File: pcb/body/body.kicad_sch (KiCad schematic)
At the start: 3 parts, among them J1 Conn_01x08_Socket, J2 Conn_01x05_Pin, U1 Teensy4.1

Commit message: output stage
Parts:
- removed U1: Teensy4.1, symbol teensy:Teensy4.1
- added A1: Electrosmith_Daisy_Seed_Rev4, Module:Electrosmith_Daisy_Seed, symbol MCU_Module:Electrosmith_Daisy_Seed_Rev4
- added J3, J4: AudioJack2, symbol Connector_Audio:AudioJack2
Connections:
- net GND: now also J3.S, J4.S
- net PICKUP_1: now also A1.22 (ADC_0)
- new net PICKUP_2: A1.23 (ADC_1)
- new net PICKUP_3: A1.24 (ADC_2)
- new net PICKUP_4: A1.25 (ADC_3)
- new net PICKUP_5: A1.26 (ADC_4)
- new net PICKUP_6: A1.27 (ADC_5)
- new net outputstage/INPUT_1: A1.18 (AUDIO_OUT_1)
- new net outputstage/INPUT_2: A1.19 (AUDIO_OUT_2)
- new net outputstage/OUTPUT_1: J3.T
- new net outputstage/OUTPUT_2: J4.T
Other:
- added sheet outputstage (outputstage.kicad_sch)
- moved on the sheet: J1

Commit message: pcb stuff
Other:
- added sheet codec1 (codec.kicad_sch)
- added sheet codec2 (codec.kicad_sch)
- added sheet codec3 (codec.kicad_sch)
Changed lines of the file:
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@@
+    )
+  )
+  (sheet (at 27.94 111.76) (size 27.94 15.24) (fields_autoplaced)
+    (stroke (width 0.1524) (type solid))
+    (fill (color 0 0 0 0.0000))
+    (property "Sheetname" "codec1" (at 27.94 111.0484 0)
+      (effects (font (size 1.27 1.27)) (justify left bottom))
+    )
+    (property "Sheetfile" "codec.kicad_sch" (at 27.94 127.5846 0)
+      (effects (font (size 1.27 1.27)) (justify left top))
+    )
+    (pin "LINE_IN_L" input (at 27.94 114.3 180)
+      (effects (font (size 1.27 1.27)) (justify left))
+    )
+    (pin "DAC_DOUT" output (at 55.88 114.3 0)
+      (effects (font (size 1.27 1.27)) (justify right))
+    )
+    (pin "DAC_DIN" input (at 55.88 116.84 0)
+      (effects (font (size 1.27 1.27)) (justify right))
+    )
+    (pin "LINE_IN_R" input (at 27.94 116.84 180)
+      (effects (font (size 1.27 1.27)) (justify left))
+    )
+    (pin "LINE_OUT_R" output (at 27.94 119.38 180)
+      (effects (font (size 1.27 1.27)) (justify left))
+    )
+    (pin "LINE_OUT_L" output (at 27.94 121.92 180)
+      (effects (font (size 1.27 1.27)) (justify left))
+    )
+    (instances
+      (project "body"
+        (path "/392bd065-a607-4eff-83a3-798a3e7c56fd" (page "6"))
+      )
     )
   )
@@
       )
     )
+  )
+  (sheet (at 27.94 133.35) (size 27.94 15.24) (fields_autoplaced)
+    (stroke (width 0.1524) (type solid))
+    (fill (color 0 0 0 0.0000))
+    (property "Sheetname" "codec2" (at 27.94 132.6384 0)
+      (effects (font (size 1.27 1.27)) (justify left bottom))
+    )
+    (property "Sheetfile" "codec.kicad_sch" (at 27.94 149.1746 0)
+      (effects (font (size 1.27 1.27)) (justify left top))
+    )
+    (instances
+      (project "body"
+        (path "/392bd065-a607-4eff-83a3-798a3e7c56fd" (page "7"))
+      )
+    )
+  )
+  (sheet (at 27.94 154.94) (size 27.94 15.24) (fields_autoplaced)
+    (stroke (width 0.1524) (type solid))
+    (fill (color 0 0 0 0.0000))
+    (property "Sheetname" "codec3" (at 27.94 154.2284 0)
+      (effects (font (size 1.27 1.27)) (justify left bottom))
+    )
+    (property "Sheetfile" "codec.kicad_sch" (at 27.94 170.7646 0)
+      (effects (font (size 1.27 1.27)) (justify left top))
+    )
+    (instances
+      (project "body"
+        (path "/392bd065-a607-4eff-83a3-798a3e7c56fd" (page "8"))
+      )
+    )

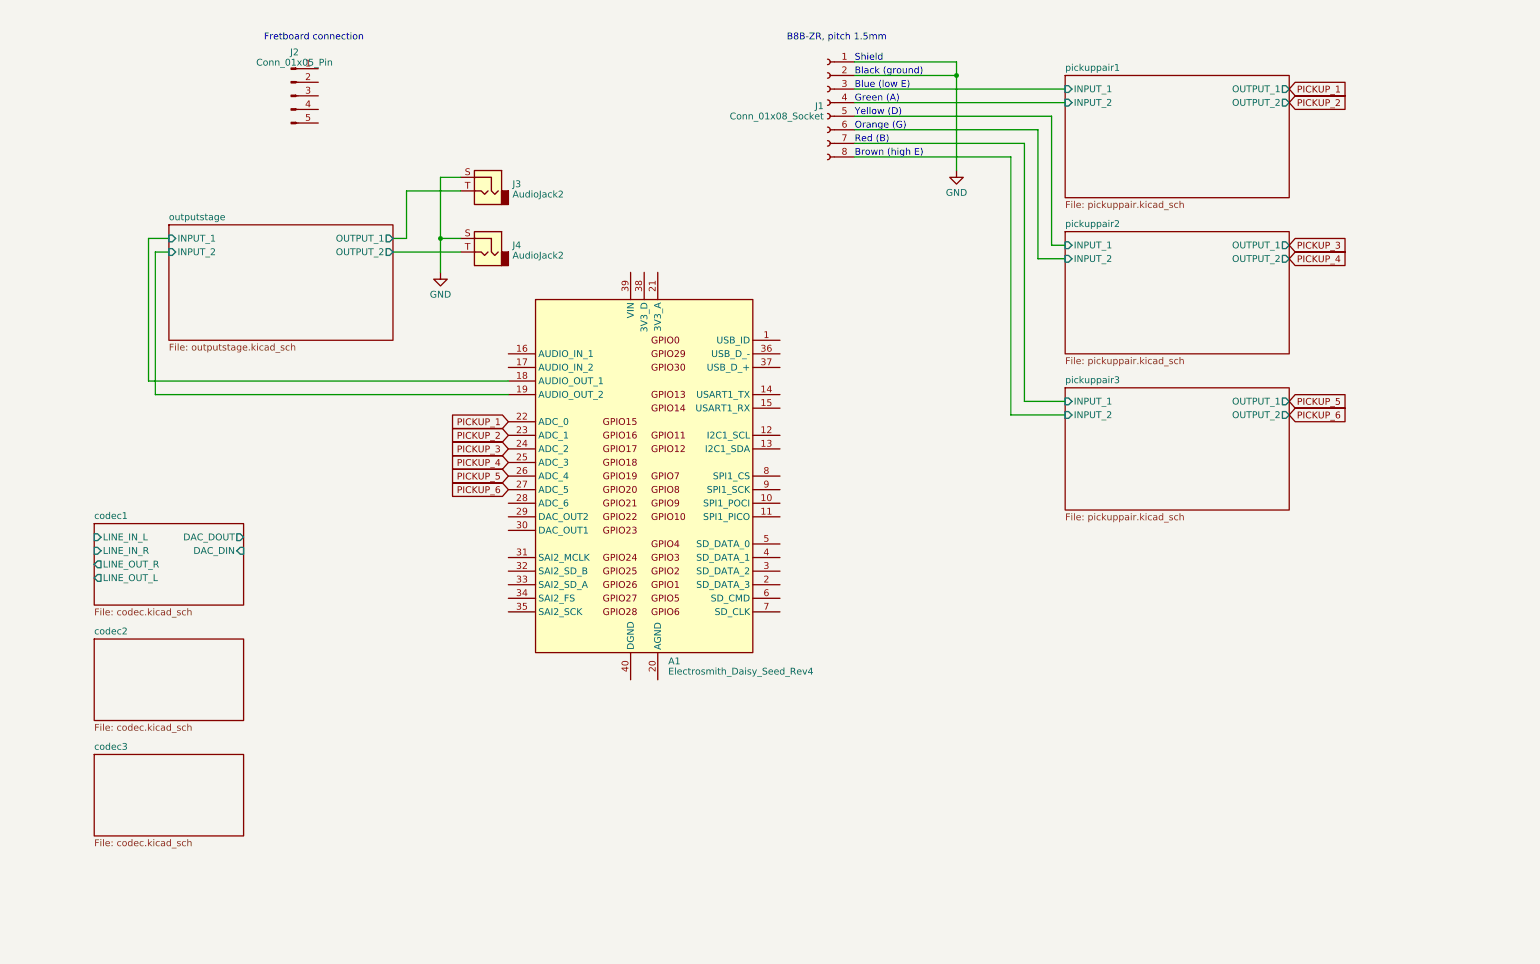
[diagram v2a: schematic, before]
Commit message: linked input stages to codecs
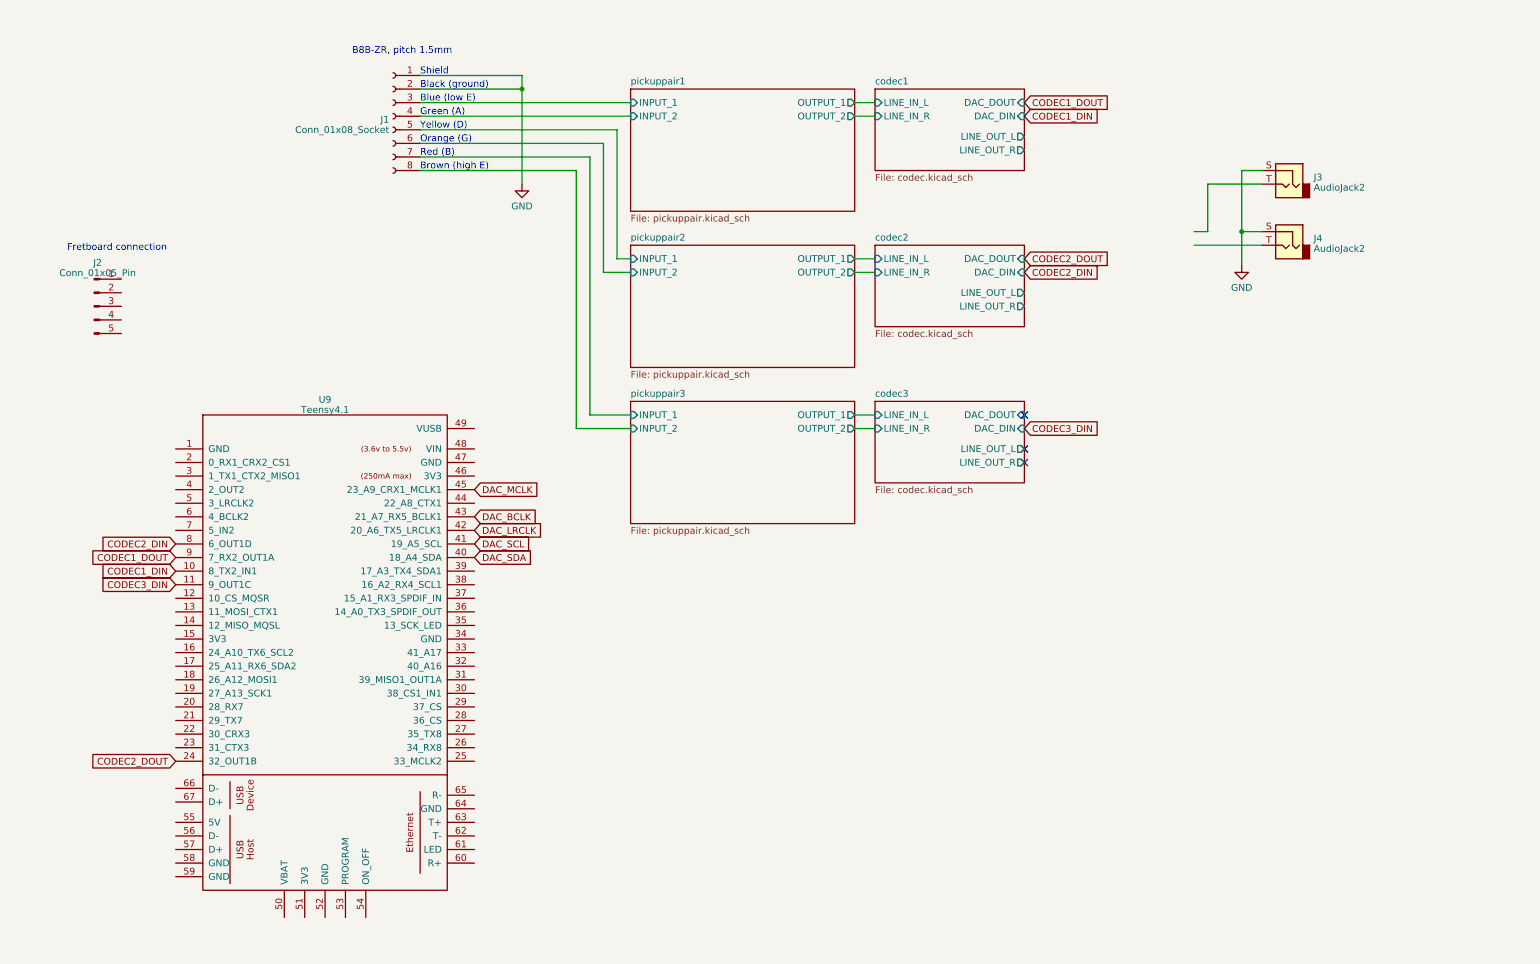
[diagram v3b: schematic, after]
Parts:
- removed A1: Electrosmith_Daisy_Seed_Rev4, Module:Electrosmith_Daisy_Seed, symbol MCU_Module:Electrosmith_Daisy_Seed_Rev4
- added U9: Teensy4.1, symbol teensy:Teensy4.1
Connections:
- net outputstage/OUTPUT_1: no longer names the net of J3.T
- net outputstage/OUTPUT_2: no longer names the net of J4.T
- new net CODEC1_DIN: U9.10 (8_TX2_IN1)
- new net CODEC1_DOUT: U9.9 (7_RX2_OUT1A)
- new net CODEC2_DIN: U9.8 (6_OUT1D)
- new net CODEC2_DOUT: U9.24 (32_OUT1B)
- new net CODEC3_DIN: U9.11 (9_OUT1C)
- new net DAC_BCLK: U9.43 (21_A7_RX5_BCLK1)
- new net DAC_LRCLK: U9.42 (20_A6_TX5_LRCLK1)
- new net DAC_MCLK: U9.45 (23_A9_CRX1_MCLK1)
- new net DAC_SCL: U9.41 (19_A5_SCL)
- new net DAC_SDA: U9.40 (18_A4_SDA)
- no-connect marks 0 -> 3
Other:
- removed sheet outputstage
- sheet codec2 ports: added DAC_DIN, DAC_DOUT, LINE_IN_L, LINE_IN_R, LINE_OUT_L, LINE_OUT_R; removed none
- sheet codec3 ports: added DAC_DIN, DAC_DOUT, LINE_IN_L, LINE_IN_R, LINE_OUT_L, LINE_OUT_R; removed none
- moved on the sheet: J1, J2, J3, J4

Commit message: not much
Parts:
- removed J3, J4: AudioJack2, symbol Connector_Audio:AudioJack2
- added J3, J4: Conn_01x04, symbol Connector_Generic:Conn_01x04
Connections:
- net GND: now also J3.2 (Pin_2), J3.3 (Pin_3), J4.2 (Pin_2), J4.3 (Pin_3)
- net codec1/LINE_OUT_L: now also J3.1 (Pin_1)
- net codec1/LINE_OUT_R: now also J3.4 (Pin_4)
- net codec2/LINE_OUT_L: now also J4.1 (Pin_1)
- net codec2/LINE_OUT_R: now also J4.4 (Pin_4)
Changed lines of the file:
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@@
 (kicad_sch (version 20230121) (generator eeschema)
   (paper "A4")
-  (junction (at 242.57 57.15) (diameter 0) (color 0 0 0 0)
-  )
   (junction (at 107.95 30.48) (diameter 0) (color 0 0 0 0)
+  )
+  (junction (at 227.33 44.45) (diameter 0) (color 0 0 0 0)
+  )
+  (junction (at 227.33 71.12) (diameter 0) (color 0 0 0 0)
+  )
+  (junction (at 227.33 73.66) (diameter 0) (color 0 0 0 0)
   )
   (no_connect (at 201.93 97.79))
@@
     (stroke (width 0) (type default))
   )
+  (wire (pts (xy 227.33 73.66) (xy 229.87 73.66))
+    (stroke (width 0) (type default))
+  )
   (wire (pts (xy 120.65 91.44) (xy 128.27 91.44))
     (stroke (width 0) (type default))
   )
-  (wire (pts (xy 246.38 45.72) (xy 242.57 45.72))
-    (stroke (width 0) (type default))
-  )
-  (wire (pts (xy 236.22 57.15) (xy 236.22 48.26))
+  (wire (pts (xy 208.28 71.12) (xy 208.28 76.2))
+    (stroke (width 0) (type default))
+  )
+  (wire (pts (xy 201.93 68.58) (xy 229.87 68.58))
     (stroke (width 0) (type default))
   )
@@
     (stroke (width 0) (type default))
   )
-  (wire (pts (xy 242.57 45.72) (xy 242.57 57.15))
+  (wire (pts (xy 227.33 44.45) (xy 227.33 71.12))
     (stroke (width 0) (type default))
   )
@@
     (stroke (width 0) (type default))
   )
+  (wire (pts (xy 227.33 73.66) (xy 227.33 80.01))
+    (stroke (width 0) (type default))
+  )
   (wire (pts (xy 123.19 40.64) (xy 123.19 64.77))
     (stroke (width 0) (type default))
@@
     (stroke (width 0) (type default))
   )
-  (wire (pts (xy 242.57 57.15) (xy 242.57 63.5))
-    (stroke (width 0) (type default))
-  )
   (wire (pts (xy 170.18 64.77) (xy 173.99 64.77))
     (stroke (width 0) (type default))
   )
+  (wire (pts (xy 227.33 41.91) (xy 227.33 44.45))
+    (stroke (width 0) (type default))
+  )
   (wire (pts (xy 170.18 91.44) (xy 173.99 91.44))
     (stroke (width 0) (type default))
@@
     (stroke (width 0) (type default))
   )
-  (wire (pts (xy 233.68 59.69) (xy 246.38 59.69))
-    (stroke (width 0) (type default))
-  )
   (wire (pts (xy 88.9 30.48) (xy 107.95 30.48))
     (stroke (width 0) (type default))
   )
-  (wire (pts (xy 233.68 57.15) (xy 236.22 57.15))
-    (stroke (width 0) (type default))
-  )
-  (wire (pts (xy 242.57 57.15) (xy 246.38 57.15))
+  (wire (pts (xy 208.28 76.2) (xy 229.87 76.2))
     (stroke (width 0) (type default))
   )
@@
     (stroke (width 0) (type default))
   )
-  (wire (pts (xy 236.22 48.26) (xy 246.38 48.26))
+  (wire (pts (xy 208.28 46.99) (xy 229.87 46.99))
+    (stroke (width 0) (type default))
+  )
+  (wire (pts (xy 227.33 44.45) (xy 229.87 44.45))
     (stroke (width 0) (type default))
   )
@@
     (stroke (width 0) (type default))
   )
+  (wire (pts (xy 227.33 71.12) (xy 227.33 73.66))
+    (stroke (width 0) (type default))
+  )
   (wire (pts (xy 88.9 35.56) (xy 128.27 35.56))
     (stroke (width 0) (type default))
@@
     (stroke (width 0) (type default))
   )
+  (wire (pts (xy 201.93 41.91) (xy 208.28 41.91))
+    (stroke (width 0) (type default))
+  )
   (wire (pts (xy 123.19 64.77) (xy 128.27 64.77))
     (stroke (width 0) (type default))
@@
     (stroke (width 0) (type default))
   )
+  (wire (pts (xy 208.28 41.91) (xy 208.28 46.99))
+    (stroke (width 0) (type default))
+  )
+  (wire (pts (xy 229.87 41.91) (xy 227.33 41.91))
+    (stroke (width 0) (type default))
+  )
+  (wire (pts (xy 201.93 39.37) (xy 229.87 39.37))
+    (stroke (width 0) (type default))
+  )
+  (wire (pts (xy 227.33 71.12) (xy 229.87 71.12))
+    (stroke (width 0) (type default))
+  )
   (wire (pts (xy 107.95 30.48) (xy 107.95 48.26))
+    (stroke (width 0) (type default))
+  )
+  (wire (pts (xy 201.93 71.12) (xy 208.28 71.12))
     (stroke (width 0) (type default))
   )
@@
     )
   )
+  (symbol (lib_id "Connector_Generic:Conn_01x04") (at 234.95 41.91 0) (unit 1)
+    (in_bom yes) (on_board yes) (dnp no) (fields_autoplaced)
+    (property "Reference" "J3" (at 237.49 42.545 0)
+      (effects (font (size 1.27 1.27)) (justify left))
+    )
+    (property "Value" "Conn_01x04" (at 237.49 45.085 0)
+      (effects (font (size 1.27 1.27)) (justify left))
+    )
+    (property "Footprint" "" (at 234.95 41.91 0)
+      (effects (font (size 1.27 1.27)) hide)
+    )
+    (property "Datasheet" "~" (at 234.95 41.91 0)
+      (effects (font (size 1.27 1.27)) hide)
+    )
+    (pin "1")
+    (pin "2")
+    (pin "3")
+    (pin "4")
+    (instances
+      (project "body"
+        (path "/392bd065-a607-4eff-83a3-798a3e7c56fd"
+          (reference "J3") (unit 1)
+        )
+      )
+    )
+  )
   (symbol (lib_id "power:GND") (at 107.95 48.26 0) (unit 1)
     (in_bom yes) (on_board yes) (dnp no) (fields_autoplaced)
@@
         (path "/392bd065-a607-4eff-83a3-798a3e7c56fd"
           (reference "J2") (unit 1)
+        )
+      )
+    )
+  )
+  (symbol (lib_id "Connector_Generic:Conn_01x04") (at 234.95 71.12 0) (unit 1)
+    (in_bom yes) (on_board yes) (dnp no) (fields_autoplaced)
+    (property "Reference" "J4" (at 237.49 71.755 0)
+      (effects (font (size 1.27 1.27)) (justify left))
+    )
+    (property "Value" "Conn_01x04" (at 237.49 74.295 0)
+      (effects (font (size 1.27 1.27)) (justify left))
+    )
+    (property "Footprint" "" (at 234.95 71.12 0)
+      (effects (font (size 1.27 1.27)) hide)
+    )
+    (property "Datasheet" "~" (at 234.95 71.12 0)
+      (effects (font (size 1.27 1.27)) hide)
+    )
+    (pin "1")
+    (pin "2")
+    (pin "3")
+    (pin "4")
+    (instances
+      (project "body"
+        (path "/392bd065-a607-4eff-83a3-798a3e7c56fd"
+          (reference "J4") (unit 1)
         )
       )
@@
     )
   )
-  (symbol (lib_id "power:GND") (at 242.57 63.5 0) (unit 1)
-    (in_bom yes) (on_board yes) (dnp no) (fields_autoplaced)
-    (property "Reference" "#PWR017" (at 242.57 69.85 0)
-      (effects (font (size 1.27 1.27)) hide)
-    )
-    (property "Value" "GND" (at 242.57 67.6355 0)
-      (effects (font (size 1.27 1.27)))
-    )
-    (property "Footprint" "" (at 242.57 63.5 0)
-      (effects (font (size 1.27 1.27)) hide)
-    )
-    (property "Datasheet" "" (at 242.57 63.5 0)
+  (symbol (lib_id "power:GND") (at 227.33 80.01 0) (unit 1)
+    (in_bom yes) (on_board yes) (dnp no) (fields_autoplaced)
+    (property "Reference" "#PWR017" (at 227.33 86.36 0)
+      (effects (font (size 1.27 1.27)) hide)
+    )
+    (property "Value" "GND" (at 227.33 84.1455 0)
+      (effects (font (size 1.27 1.27)))
+    )
+    (property "Footprint" "" (at 227.33 80.01 0)
+      (effects (font (size 1.27 1.27)) hide)
+    )
+    (property "Datasheet" "" (at 227.33 80.01 0)
       (effects (font (size 1.27 1.27)) hide)
     )
@@
         )
       )
-    )
-  )
-  (symbol (lib_id "Connector_Audio:AudioJack2") (at 251.46 59.69 0) (mirror y) (unit 1)
-    (in_bom yes) (on_board yes) (dnp no) (fields_autoplaced)
-    (property "Reference" "J4" (at 256.032 58.4113 0)
-      (effects (font (size 1.27 1.27)) (justify right))
-    )
-    (property "Value" "AudioJack2" (at 256.032 60.3323 0)
-      (effects (font (size 1.27 1.27)) (justify right))
-    )
-    (property "Footprint" "" (at 251.46 59.69 0)
-      (effects (font (size 1.27 1.27)) hide)
-    )
-    (property "Datasheet" "~" (at 251.46 59.69 0)
-      (effects (font (size 1.27 1.27)) hide)
-    )
-    (pin "S")
-    (pin "T")
-    (instances
-      (project "body"
-        (path "/392bd065-a607-4eff-83a3-798a3e7c56fd"
-          (reference "J4") (unit 1)
-        )
-      )
-    )
-  )
-  (symbol (lib_id "Connector_Audio:AudioJack2") (at 251.46 48.26 0) (mirror y) (unit 1)
-    (in_bom yes) (on_board yes) (dnp no) (fields_autoplaced)
-    (property "Reference" "J3" (at 256.032 46.9813 0)
-      (effects (font (size 1.27 1.27)) (justify right))
-    )
-    (property "Value" "AudioJack2" (at 256.032 48.9023 0)
-      (effects (font (size 1.27 1.27)) (justify right))
-    )
-    (property "Footprint" "" (at 251.46 48.26 0)
-      (effects (font (size 1.27 1.27)) hide)
-    )
-    (property "Datasheet" "~" (at 251.46 48.26 0)
-      (effects (font (size 1.27 1.27)) hide)
-    )
-    (pin "S")
-    (pin "T")
-    (instances
-      (project "body"
-        (path "/392bd065-a607-4eff-83a3-798a3e7c56fd"
-          (reference "J3") (unit 1)
-        )
-      )

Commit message: nice progress
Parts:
- added J5: Headphones, Connector_PinHeader_2.54mm:PinHeader_1x03_P2.54mm_Vertical, symbol Connector_Generic:Conn_01x03
- added J6: AudioJack3_SwitchTR, symbol Connector_Audio:AudioJack3_SwitchTR
- J1: renamed from J2; footprint (none) -> Connector_PinHeader_2.54mm:PinHeader_1x05_P2.54mm_Horizontal
- J2: renamed from J1; footprint (none) -> Connector_Wuerth:Wuerth_WR-WTB_64800811622_1x08_P1.50mm_Vertical
- J3: value Conn_01x04 -> Output_1_2; footprint (none) -> Connector_PinHeader_2.54mm:PinHeader_1x04_P2.54mm_Vertical
- J4: value Conn_01x04 -> Output_3_4; footprint (none) -> Connector_PinHeader_2.54mm:PinHeader_1x04_P2.54mm_Vertical
- U1: renamed from U9; footprint (none) -> bjarkarbody:Teensy41_breakout; symbol teensy:Teensy4.1 -> bjarkarbody:Teensy4.1_simplified
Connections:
- no-connect marks 3 -> 9
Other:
- added sheet Power (power.kicad_sch)
- sheet codec1 ports: added HEADPHONES_GND, HEADPHONES_L, HEADPHONES_R; removed none
- sheet codec2 ports: added HEADPHONES_GND, HEADPHONES_L, HEADPHONES_R; removed none
- sheet codec3 ports: added HEADPHONES_GND, HEADPHONES_L, HEADPHONES_R; removed none

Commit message: initial layout
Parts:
- removed J5: Headphones, Connector_PinHeader_2.54mm:PinHeader_1x03_P2.54mm_Vertical, symbol Connector_Generic:Conn_01x03
- J6: footprint (none) -> Connector_Audio:Jack_3.5mm_CUI_SJ1-3525N_Horizontal
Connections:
- net codec1/HEADPHONES_GND: now also J6.S
- net codec1/HEADPHONES_L: now also J6.T
- net codec1/HEADPHONES_R: now also J6.R
- no-connect marks 9 -> 11
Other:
- moved on the sheet: J3, J4, J6
